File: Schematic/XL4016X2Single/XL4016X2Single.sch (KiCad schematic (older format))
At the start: 71 parts, among them J1 Solar panel, J2 Buck1_IN, J3 LOAD, J4 Buck1_OUT, J5 Buck2_IN, J6 Buck2_OUT, J7 Battery, J8 Temperature, J9 Jack-DC, Q1 IRF4905, Q10 IRF4905, Q11 2N3906, Q12 2N3906, Q13 2N3904, Q2 IRF4905, Q3 2N3906, Q4 2N3906, Q5 2N3904, Q6 IRF4905, Q7 2N3906, Q8 2N3906, Q9 IRF4905, SW1 Backlight control, U1 XL4016_DC-DC_module, U10 AMS1117-33, U2 ACS712module, U3 XL4016_DC-DC_module, U4 ACS712module, U5 MP2307_DC-DC_module, U6 LCDSerial2004, U7 DS18B20, U8 ArduinoNano, U9 ESP-01

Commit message: minor fixes to shematic; progressed Fritzing but not finished yet
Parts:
- removed Q1, Q10, Q2, Q6, Q9: IRF4905, symbol Q_PMOS_DGS
- added Q1, Q10, Q2, Q3, Q9: IRF4905, TO_SOT_Packages_THT:TO-220_Vertical, symbol IRF4905
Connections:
- wire segments 128 -> 156
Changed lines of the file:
@@
 $EndComp
 Wire Wire Line
-	1350 1050 1850 1050
-Wire Wire Line
-	900  750  2100 750
+	1350 1050 1550 1050
+Wire Wire Line
+	1550 1050 1850 1050
+Wire Wire Line
+	900  750  1100 750
+Wire Wire Line
+	1100 750  1350 750
+Wire Wire Line
+	1350 750  2100 750
 $Comp
 L GND #PWR4
@@
 Connection ~ 9800 3650
 Wire Wire Line
-	2550 750  4500 750
+	2550 750  2900 750
+Wire Wire Line
+	2900 750  3400 750
+Wire Wire Line
+	3400 750  4500 750
 $Comp
 L XL4016_DC-DC_module U3
@@
 $EndComp
 Wire Wire Line
-	3800 850  4500 850
+	3800 850  4150 850
+Wire Wire Line
+	4150 850  4500 850
 Wire Wire Line
 	4500 1050 4150 1050
@@
 $EndComp
 Wire Wire Line
-	3800 1900 4500 1900
+	3800 1900 4150 1900
+Wire Wire Line
+	4150 1900 4500 1900
 Wire Wire Line
 	4150 2100 4150 1900
@@
 Arduino_pin_D2
 Wire Wire Line
-	1000 6450 2450 6450
+	1000 6450 2300 6450
+Wire Wire Line
+	2300 6450 2450 6450
 $Comp
 L GND #PWR18
@@
 $EndComp
 Wire Wire Line
-	1900 6150 2350 6150
+	1900 6150 2300 6150
+Wire Wire Line
+	2300 6150 2350 6150
 Wire Wire Line
 	1900 6350 1900 6150
@@
 Connection ~ 1100 750
 $Comp
-L Q_PMOS_DGS Q2
-U 1 1 5ACD8ADE
-P 10100 900
-F 0 "Q2" V 10300 700 50  0000 L CNN
-F 1 "IRF4905" V 10300 850 50  0000 L CNN
-F 2 "" H 10300 1000 50  0001 C CNN
-F 3 "" H 10100 900 50  0001 C CNN
-	1    10100 900
-	0    1    -1   0
-$EndComp
-$Comp
 L R R2
 U 1 1 5ACD8ADF
@@
 $EndComp
 Wire Wire Line
+	7700 800  7850 800
+Wire Wire Line
+	7850 800  8250 800
+Wire Wire Line
 	8250 800  9900 800
 Wire Wire Line
@@
 	10100 1100 9600 1100
 $Comp
-L Q_PMOS_DGS Q6
-U 1 1 5ACD8AE3
-P 7500 2300
-F 0 "Q6" V 7700 2150 50  0000 L CNN
-F 1 "IRF4905" V 7650 2350 50  0000 L CNN
-F 2 "" H 7700 2400 50  0001 C CNN
-F 3 "" H 7500 2300 50  0001 C CNN
-	1    7500 2300
-	0    -1   -1   0
-$EndComp
-$Comp
 L R R11
 U 1 1 5ACD8AE4
@@
 $EndComp
 Wire Wire Line
-	4550 5350 10600 5350
+	4550 5350 6150 5350
+Wire Wire Line
+	6150 5350 6950 5350
+Wire Wire Line
+	6950 5350 8250 5350
+Wire Wire Line
+	8250 5350 8800 5350
+Wire Wire Line
+	8800 5350 10600 5350
 $Comp
 L GND #PWR14
@@
 Text Notes 3250 3350 0    60   ~ 0
 MAINS SUPPLY CONTROL SUB-CIRCUIT
-$Comp
-L Q_PMOS_DGS Q10
-U 1 1 5ACD8AE8
-P 6150 3650
-F 0 "Q10" V 6350 3500 50  0000 L CNN
-F 1 "IRF4905" V 6300 3700 50  0000 L CNN
-F 2 "" H 6350 3750 50  0001 C CNN
-F 3 "" H 6150 3650 50  0001 C CNN
-	1    6150 3650
-	0    1    -1   0
-$EndComp
 Text GLabel 2050 3550 0    60   Input ~ 0
 Mains_Adapter_+12V_3A
@@
 	7700 2200 8250 2200
 Wire Wire Line
-	7500 3550 9500 3550
-Wire Wire Line
-	8250 800  8250 3450
+	7500 3550 8800 3550
+Wire Wire Line
+	8800 3550 9500 3550
+Wire Wire Line
+	8250 800  8250 2200
+Wire Wire Line
+	8250 2200 8250 3450
 Wire Wire Line
 	6150 3850 5950 3850
@@
 Wire Wire Line
 	7500 2900 7850 2900
-$Comp
-L Q_PMOS_DGS Q9
-U 1 1 5ACD8AF0
-P 5200 3650
-F 0 "Q9" V 5400 3500 50  0000 L CNN
-F 1 "IRF4905" V 5350 3700 50  0000 L CNN
-F 2 "" H 5400 3750 50  0001 C CNN
-F 3 "" H 5200 3650 50  0001 C CNN
-	1    5200 3650
-	0    -1   -1   0
-$EndComp
 Wire Wire Line
 	5400 3550 5950 3550
 Wire Wire Line
-	2500 3550 5000 3550
+	2500 3550 4700 3550
+Wire Wire Line
+	4700 3550 5000 3550
 $Comp
 L GND #PWR13
@@
 Wire Wire Line
 	4450 4850 5550 4850
-$Comp
-L Q_PMOS_DGS Q1
-U 1 1 5ACD8AF8
-P 7500 900
-F 0 "Q1" V 7700 750 50  0000 L CNN
-F 1 "IRF4905" V 7650 950 50  0000 L CNN
-F 2 "" H 7700 1000 50  0001 C CNN
-F 3 "" H 7500 900 50  0001 C CNN
-	1    7500 900
-	0    -1   -1   0
-$EndComp
 Wire Wire Line
 	6500 800  7300 800
@@
 	8050 2100 8050 3400
 Wire Notes Line
-	8050 3350 6800 3350
+	8050 3400 6800 3400
 Wire Notes Line
 	6800 3400 6800 2100
@@
 $EndComp
 Wire Wire Line
-	8050 3850 8050 5050
+	8050 3850 8050 4650
+Wire Wire Line
+	8050 4650 8050 5050
 Wire Wire Line
 	6950 5150 6950 5350
@@
 	7900 5750 7900 4650
 Wire Wire Line
-	7900 4650 8250 4650
+	7900 4650 8050 4650
+Wire Wire Line
+	8050 4650 8250 4650
 Connection ~ 8050 4650
 $Comp
@@
 	4150 7050 3750 7050
 Wire Wire Line
-	3750 7000 3750 7200
-Wire Wire Line
-	3250 7000 3450 7000
+	3750 7000 3750 7050
+Wire Wire Line
+	3750 7050 3750 7200
+Wire Wire Line
+	3250 7000 3400 7000
+Wire Wire Line
+	3400 7000 3450 7000
 $Comp
 L GND #PWR19
@@
 Arduino_pin_A6
 Wire Wire Line
-	2900 750  2900 1950
+	2900 750  2900 1000
+Wire Wire Line
+	2900 1000 2900 1300
+Wire Wire Line
+	2900 1300 2900 1650
+Wire Wire Line
+	2900 1650 2900 1950
 Connection ~ 2900 1650
 Connection ~ 2900 1300
@@
 Connection ~ 2900 1000
 Wire Wire Line
-	3200 1000 3200 1950
+	3200 1000 3200 1300
+Wire Wire Line
+	3200 1300 3200 1650
+Wire Wire Line
+	3200 1650 3200 1950
 Connection ~ 3200 1300
 Connection ~ 3200 1650
@@
 NoConn ~ 5450 7350
 Wire Wire Line
-	1350 7100 1350 7300
+	1350 7100 1350 7200
+Wire Wire Line
+	1350 7200 1350 7300
 Connection ~ 1350 7200
 Connection ~ 3750 7050
@@
 NoConn ~ 3250 7200
 Connection ~ 1350 7300
+Connection ~ 8250 800
+Connection ~ 7850 800
+$Comp
+L IRF4905 Q2
+U 1 1 5ACEA1FB
+P 10100 900
+F 0 "Q2" V 10300 700 50  0000 L CNN
+F 1 "IRF4905" V 10300 950 50  0000 L CNN
+F 2 "TO_SOT_Packages_THT:TO-220_Vertical" H 10350 825 50  0001 L CIN
+F 3 "" H 10100 900 50  0001 L CNN
+	1    10100 900
+	0    1    -1   0
+$EndComp
+$Comp
+L IRF4905 Q1
+U 1 1 5ACEA4C3
+P 7500 900
+F 0 "Q1" V 7700 1000 50  0000 L CNN
+F 1 "IRF4905" V 7700 500 50  0000 L CNN
+F 2 "TO_SOT_Packages_THT:TO-220_Vertical" H 7750 825 50  0001 L CIN
+F 3 "" H 7500 900 50  0001 L CNN
+	1    7500 900
+	0    -1   -1   0
+$EndComp
+$Comp
+L IRF4905 Q3
+U 1 1 5ACEA89A
+P 7500 2300
+F 0 "Q3" V 7750 2400 50  0000 L CNN
+F 1 "IRF4905" V 7750 2000 50  0000 L CNN
+F 2 "TO_SOT_Packages_THT:TO-220_Vertical" H 7750 2225 50  0001 L CIN
+F 3 "" H 7500 2300 50  0001 L CNN
+	1    7500 2300
+	0    -1   -1   0
+$EndComp
+$Comp
+L IRF4905 Q10
+U 1 1 5ACEC55F
+P 6150 3650
+F 0 "Q10" V 6350 3450 50  0000 L CNN
+F 1 "IRF4905" V 6350 3650 50  0000 L CNN
+F 2 "TO_SOT_Packages_THT:TO-220_Vertical" H 6400 3575 50  0001 L CIN
+F 3 "" H 6150 3650 50  0001 L CNN
+	1    6150 3650
+	0    1    -1   0
+$EndComp
+$Comp
+L IRF4905 Q9
+U 1 1 5ACECF27
+P 5200 3650
+F 0 "Q9" V 5400 3750 50  0000 L CNN
+F 1 "IRF4905" V 5400 3300 50  0000 L CNN
+F 2 "TO_SOT_Packages_THT:TO-220_Vertical" H 5450 3575 50  0001 L CIN
+F 3 "" H 5200 3650 50  0001 L CNN
+	1    5200 3650
+	0    -1   -1   0
+$EndComp
+Connection ~ 7000 800
 $EndSCHEMATC

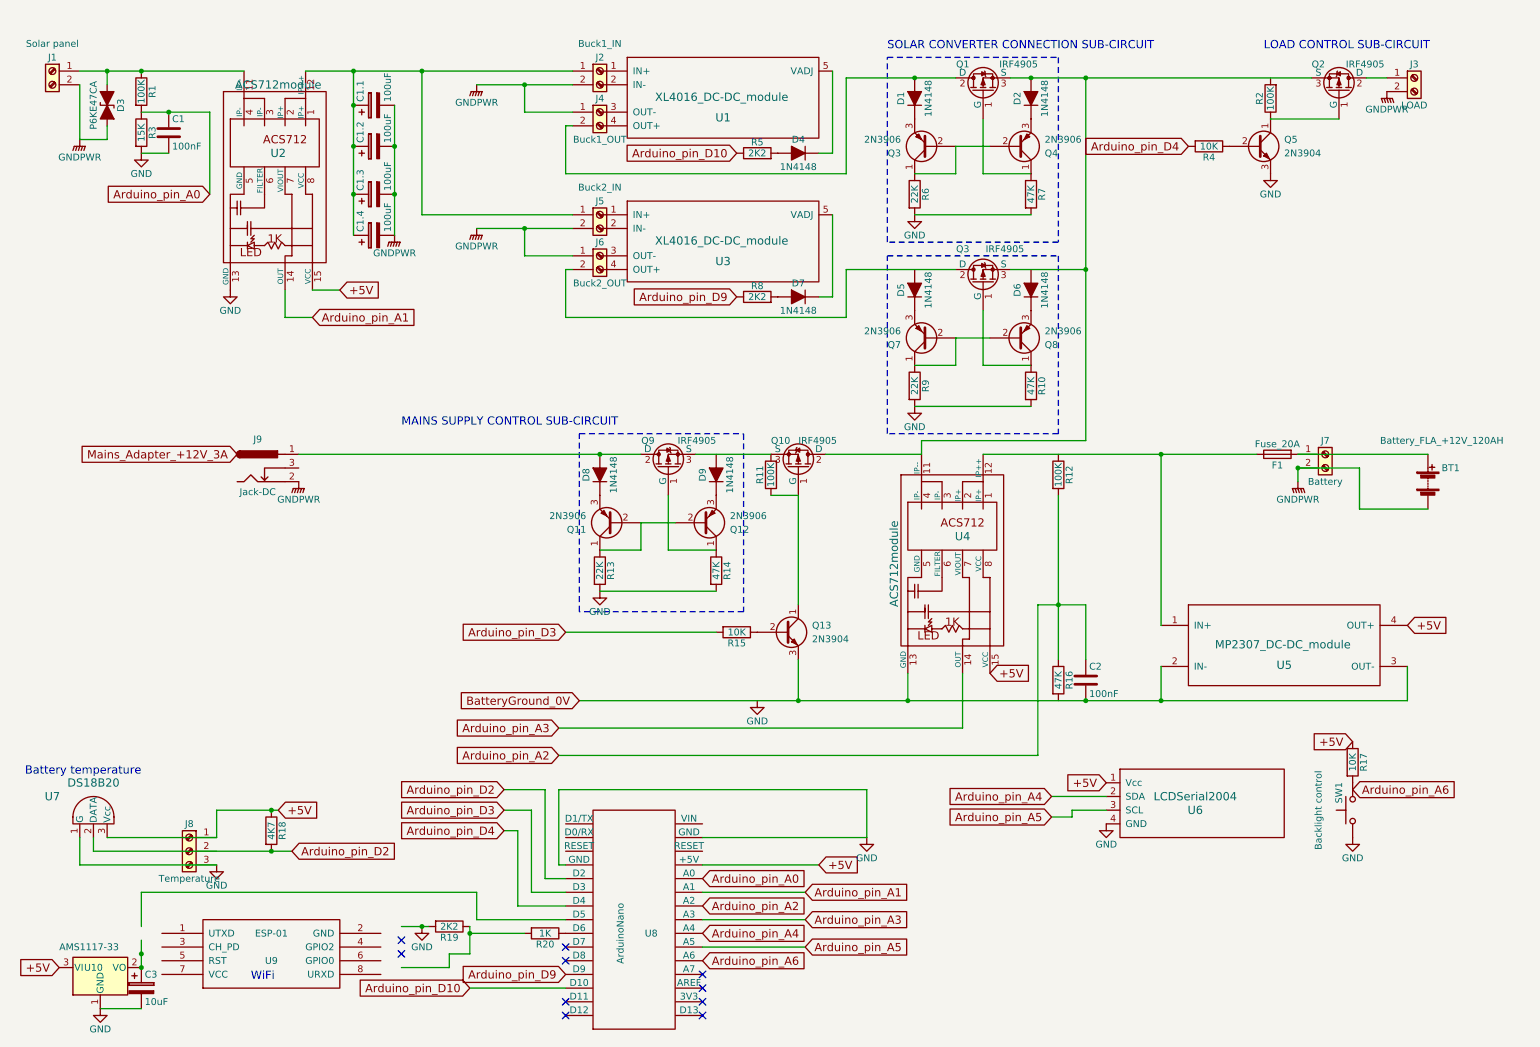
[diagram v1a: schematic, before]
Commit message: added SD and RTC modules
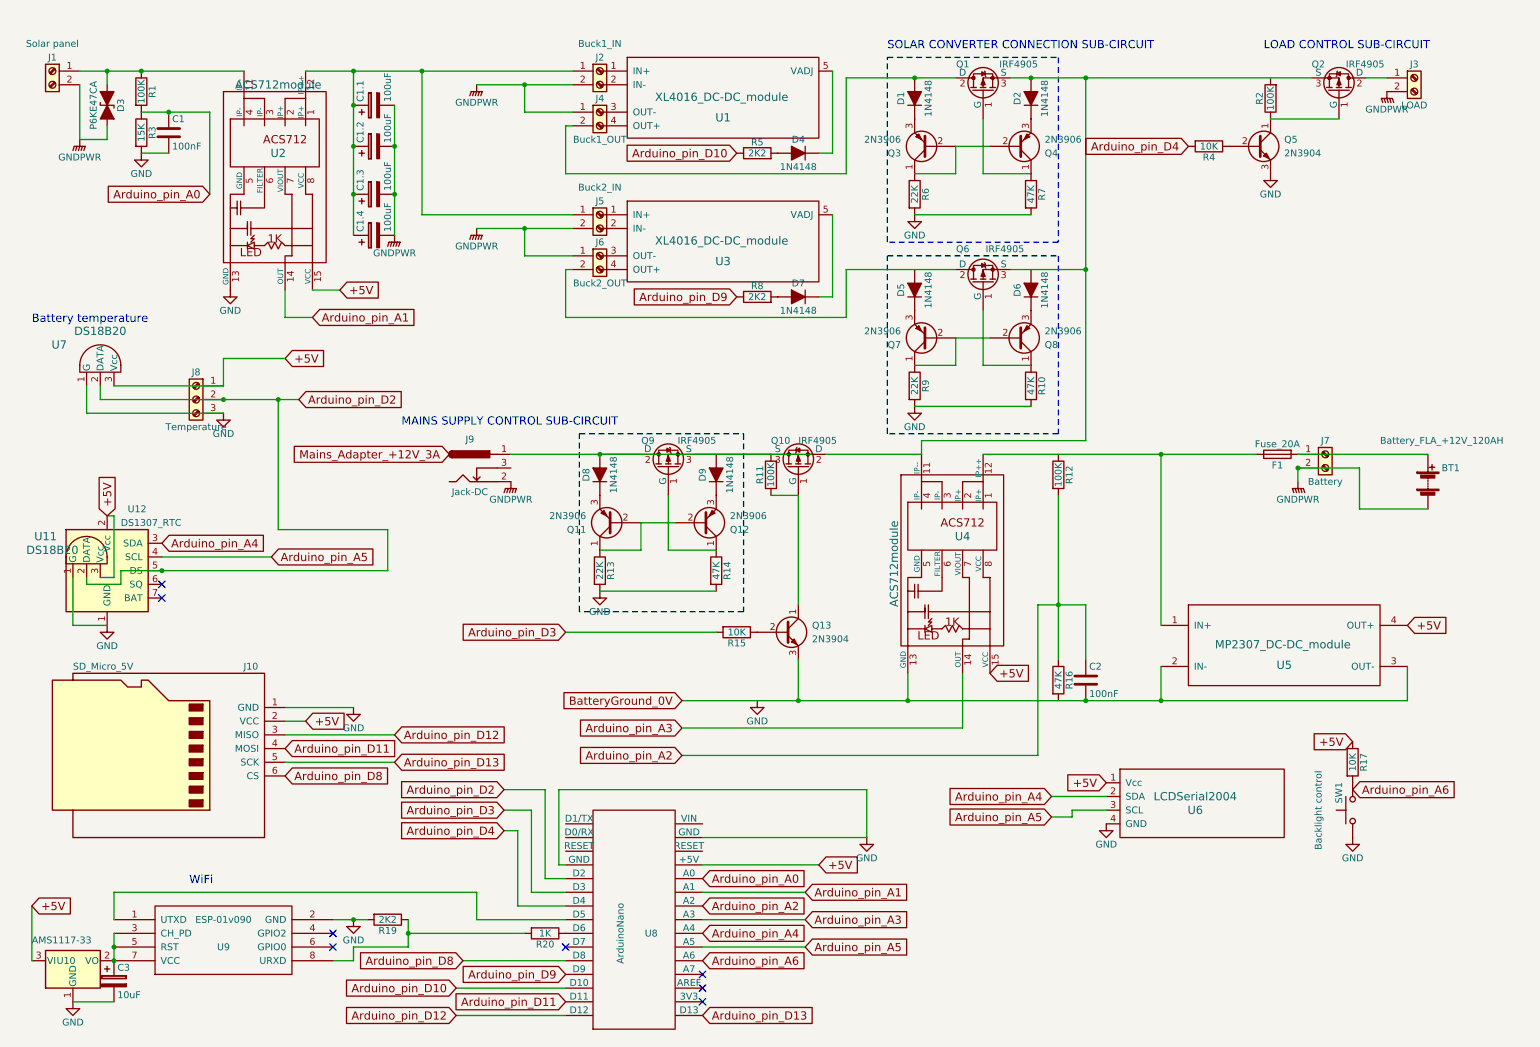
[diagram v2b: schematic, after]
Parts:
- removed R18: 4K7, symbol R
- added J10: SD_Micro_5V, symbol SD_Micro_5V
- added U11: DS18B20, symbol DS18B20
- added U12: DS1307_RTC, symbol DS1307_RTC
- U9: value ESP-01 -> ESP-01v090
- renumbered Q3 to Q6
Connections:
- net +5V: now also J10.2 (VCC), U11.3 (Vcc), U12.2 (Vcc)
- net Arduino_pin_A4: now also U12.3 (SDA)
- net Arduino_pin_A5: now also U12.4 (SCL)
- net Arduino_pin_D2: now also J8.2 (Pin_2), U11.2 (DATA), U12.5 (DS)
- net GND: now also U9.2 (GND), J10.1 (GND), U11.1 (G), U12.1 (GND)
- net at Q10.3 (S), Q9.3 (S), R11.2: now also D8.2 (A), J9.1, Q9.2 (D)
- net Arduino_pin_D8: now reaches U8.11 (D8)
- net Arduino_pin_D8: now also J10.6 (CS)
- net Arduino_pin_D11: now reaches U8.14 (D11)
- net Arduino_pin_D11: now also J10.4 (MOSI)
- net Arduino_pin_D12: now reaches U8.15 (D12)
- net Arduino_pin_D12: now also J10.3 (MISO)
- net Arduino_pin_D13: now reaches U8.16 (D13)
- net Arduino_pin_D13: now also J10.5 (SCK)
- net at U8.8 (D5): now also U9.1 (UTXD)
- net at U9.3 (CH_PD): now also C3.1, U10.2 (VO), U9.5 (RST), U9.7 (VCC)
- net at U9.8 (URXD): now also R19.1, R20.2
- no-connect marks 10 -> 8
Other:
- moved on the sheet: C3, J8, J9, R19, U10, U7

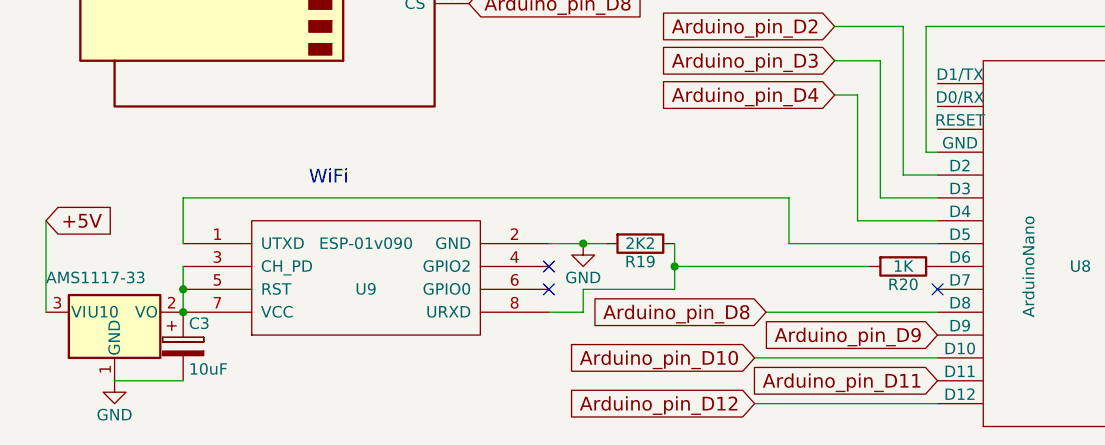
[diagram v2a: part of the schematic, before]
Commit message: deleted ESP-01 (WiFi) module
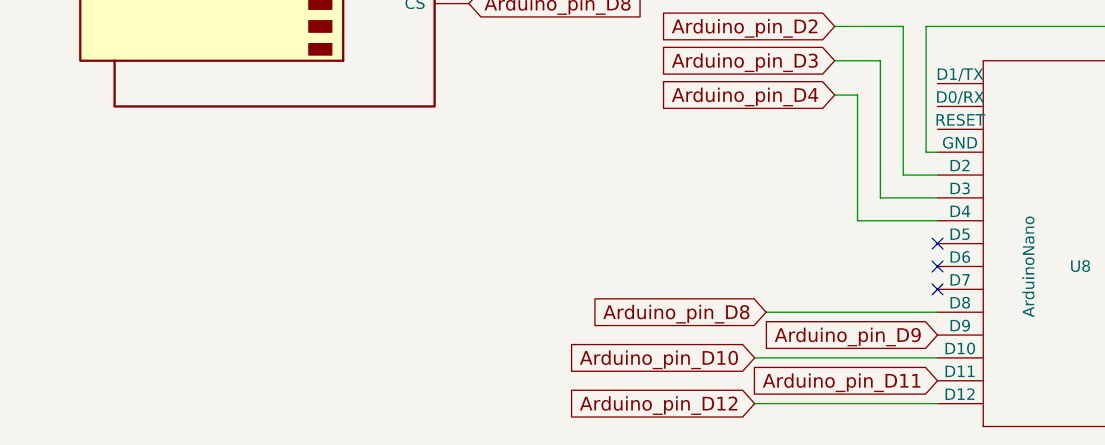
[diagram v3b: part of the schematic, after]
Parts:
- removed C3: 10uF, symbol CP
- removed R19: 2K2, symbol R
- removed R20: 1K, symbol R
- removed U10: AMS1117-33, TO_SOT_Packages_SMD:SOT-223-3Lead_TabPin2, symbol AP1117-33
- removed U9: ESP-01v090, symbol ESP-01v090
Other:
- note removed: "WiFi"
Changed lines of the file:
@@
 Wire Wire Line
 	5450 6350 6650 6350
-Wire Wire Line
-	1150 6950 1150 6750
-Wire Wire Line
-	1150 6750 3800 6750
-$Comp
-L R R20
-U 1 1 5ACDAD41
-P 4300 7050
-F 0 "R20" V 4380 7050 50  0000 C CNN
-F 1 "1K" V 4300 7050 50  0000 C CNN
-F 2 "" V 4230 7050 50  0001 C CNN
-F 3 "" H 4300 7050 50  0001 C CNN
-	1    4300 7050
-	0    1    1    0
-$EndComp
-$Comp
-L R R19
-U 1 1 5ACDAD42
-P 3150 6950
-F 0 "R19" V 3230 6950 50  0000 C CNN
-F 1 "2K2" V 3150 6950 50  0000 C CNN
-F 2 "" V 3080 6950 50  0001 C CNN
-F 3 "" H 3150 6950 50  0001 C CNN
-	1    3150 6950
-	0    1    1    0
-$EndComp
-Wire Wire Line
-	4150 7050 3300 7050
-Wire Wire Line
-	3300 6950 3300 7150
-Wire Wire Line
-	2750 6950 3000 6950
-$Comp
-L GND #PWR21
-U 1 1 5ACDAD43
-P 2900 6950
-F 0 "#PWR21" H 2900 6700 50  0001 C CNN
-F 1 "GND" H 2900 6800 50  0000 C CNN
-F 2 "" H 2900 6950 50  0001 C CNN
-F 3 "" H 2900 6950 50  0001 C CNN
-	1    2900 6950
-	1    0    0    -1
-$EndComp
-$Comp
-L AP1117-33 U10
-U 1 1 5ACDAD44
-P 850 7250
-F 0 "U10" H 800 7250 50  0000 C CNN
-F 1 "AMS1117-33" H 550 7400 50  0000 L CNN
-F 2 "TO_SOT_Packages_SMD:SOT-223-3Lead_TabPin2" H 850 7450 50  0001 C CNN
-F 3 "" H 950 7000 50  0001 C CNN
-	1    850  7250
-	1    0    0    -1
-$EndComp
-Text GLabel 550  6850 2    60   Input ~ 0
-+5V
-$Comp
-L GND #PWR22
-U 1 1 5ACDAD45
-P 850 7550
-F 0 "#PWR22" H 850 7300 50  0001 C CNN
-F 1 "GND" H 850 7400 50  0000 C CNN
-F 2 "" H 850 7550 50  0001 C CNN
-F 3 "" H 850 7550 50  0001 C CNN
-	1    850  7550
-	1    0    0    -1
-$EndComp
 Text GLabel 5450 6850 2    60   Input ~ 0
 Arduino_pin_A2
@@
 Wire Wire Line
 	3650 7450 4450 7450
-Wire Wire Line
-	4450 6950 3800 6950
-Wire Wire Line
-	3800 6950 3800 6750
 Text GLabel 4000 6150 0    60   Input ~ 0
 Arduino_pin_D3
@@
 Wire Wire Line
 	4200 6750 4450 6750
-$Comp
-L CP C3
-U 1 1 5ACDAD46
-P 1150 7400
-F 0 "C3" H 1175 7500 50  0000 L CNN
-F 1 "10uF" H 1175 7300 50  0000 L CNN
-F 2 "" H 1188 7250 50  0001 C CNN
-F 3 "" H 1150 7400 50  0001 C CNN
-	1    1150 7400
-	1    0    0    -1
-$EndComp
-Wire Wire Line
-	850  7550 1150 7550
-Text Notes 1700 6700 0    60   ~ 0
-WiFi
 Text GLabel 4000 6000 0    60   Input ~ 0
 Arduino_pin_D2
@@
 	1    0    0    -1
 $EndComp
-Connection ~ 2900 6950
 NoConn ~ 4450 7150
 NoConn ~ 5450 7550
 NoConn ~ 5450 7450
 NoConn ~ 5450 7350
-Wire Wire Line
-	1150 7050 1150 7250
-Connection ~ 1150 7150
 Connection ~ 8250 800
 Connection ~ 7850 800
@@
 Connection ~ 7000 800
 $Comp
-L ESP-01v090 U9
-U 1 1 5ACF8297
-P 1950 7050
-F 0 "U9" H 1950 6950 50  0000 C CNN
-F 1 "ESP-01v090" H 1950 7150 50  0000 C CNN
-F 2 "" H 1950 7050 50  0001 C CNN
-F 3 "" H 1950 7050 50  0001 C CNN
-	1    1950 7050
-	1    0    0    -1
-$EndComp
-NoConn ~ 2750 7050
-NoConn ~ 2750 7150
-$Comp
 L SD_Micro_5V J10
 U 1 1 5ACFE4B2
@@
 Wire Wire Line
 	2400 5800 3200 5800
-Wire Wire Line
-	550  6850 550  7250
 Text GLabel 3700 7250 0    60   Input ~ 0
 Arduino_pin_D8
 Wire Wire Line
 	4450 7250 3700 7250
-Connection ~ 1150 7250
-Wire Wire Line
-	2750 7250 2900 7250
-Wire Wire Line
-	2900 7250 2900 7150
-Wire Wire Line
-	2900 7150 3300 7150
-Connection ~ 3300 7050
 Text GLabel 2400 5900 2    60   Input ~ 0
 Arduino_pin_D8
@@
 NoConn ~ 1500 4500
 NoConn ~ 1500 4600
+NoConn ~ 4450 7050
+NoConn ~ 4450 6950
 $EndSCHEMATC
